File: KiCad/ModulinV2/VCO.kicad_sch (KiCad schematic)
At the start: 87 parts, among them Q1 MMBFJ201, Q2 MMBFJ201, SW3 SW_SPDT_MSM

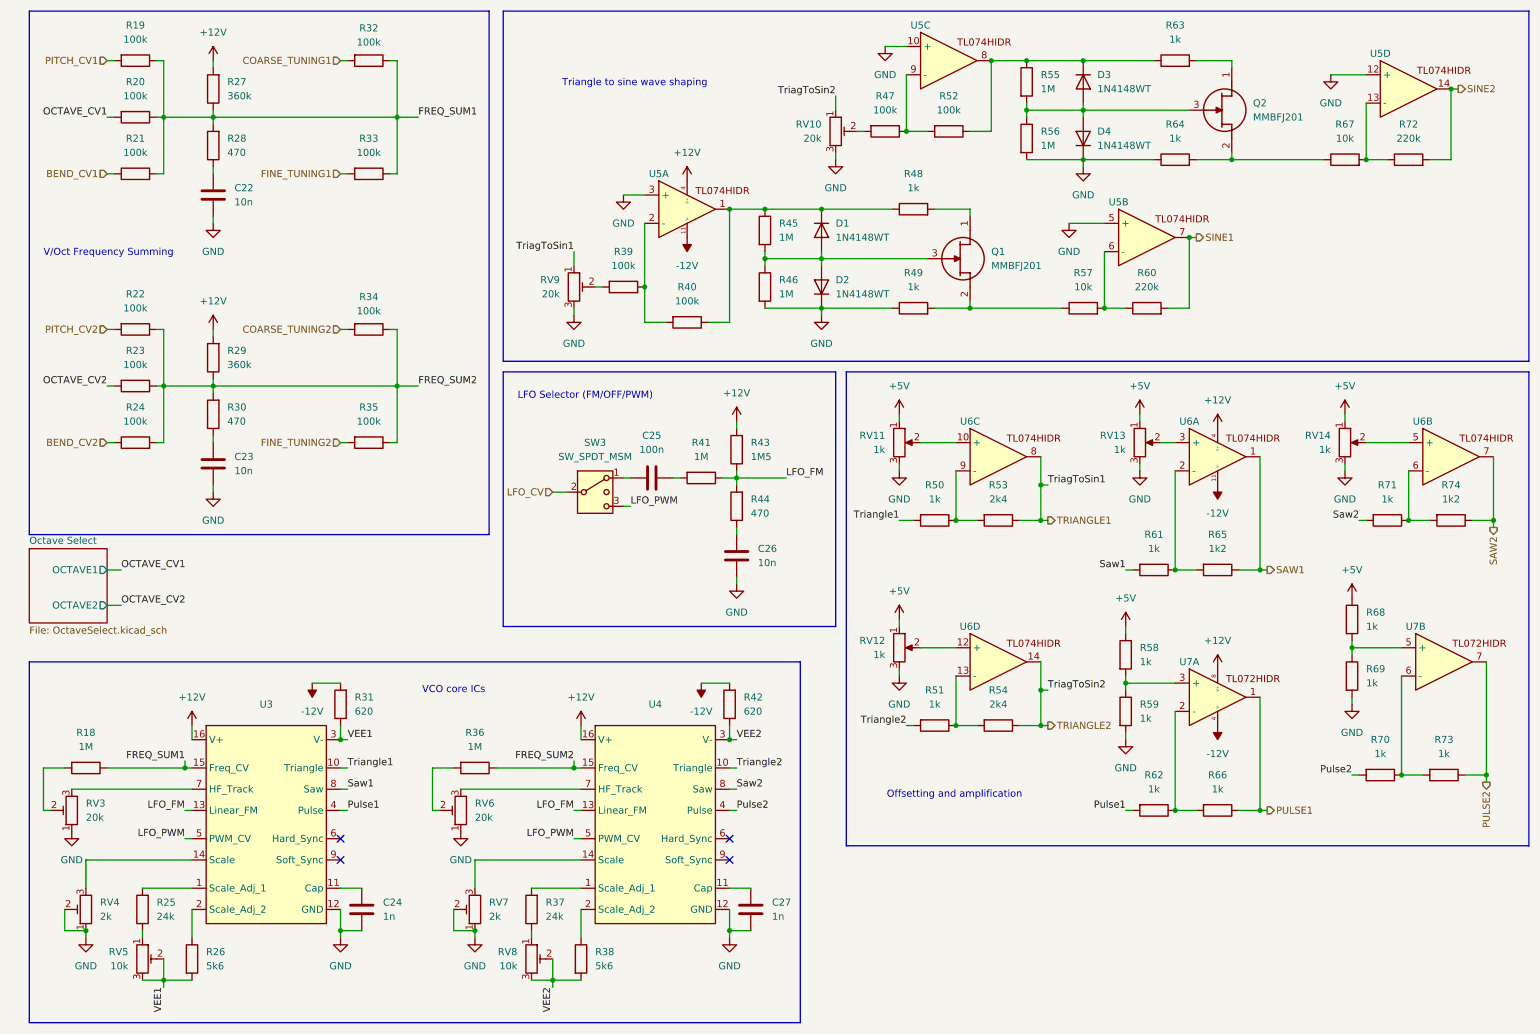
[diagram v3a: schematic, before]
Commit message: Fleshed out the waveform select schematic a bit + general cleanup
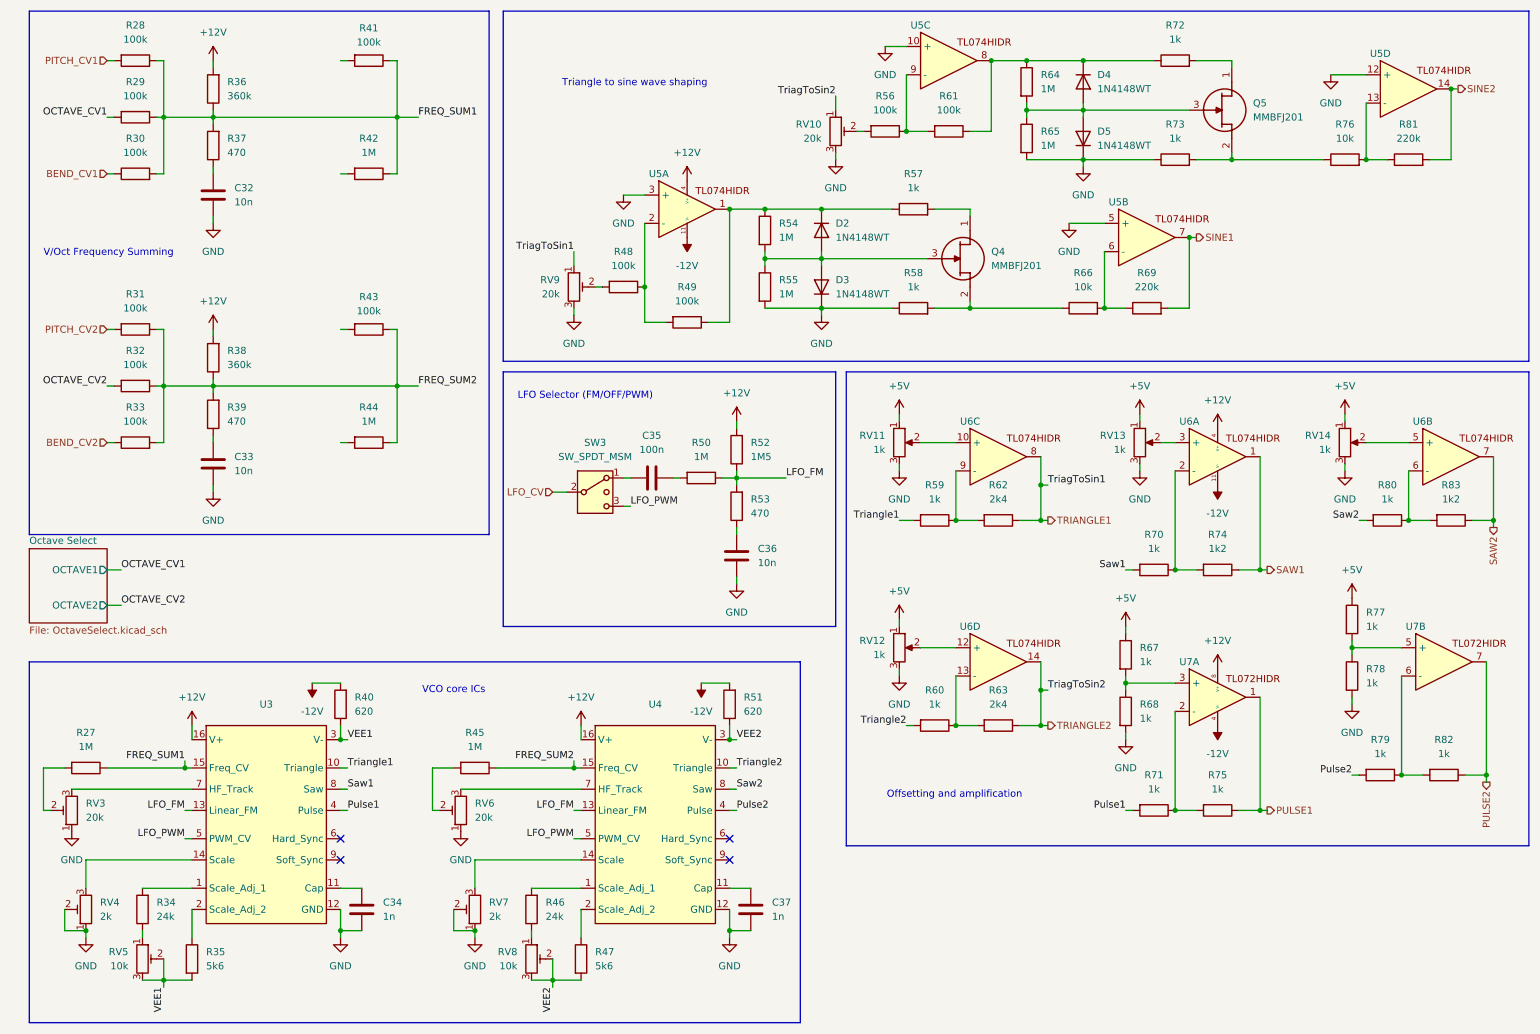
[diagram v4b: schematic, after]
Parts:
- R42: renamed from R33; value 100k -> 1M
- R44: renamed from R35; value 100k -> 1M
- renumbered C22 to C32, C23 to C33, C24 to C34, C25 to C35, C26 to C36, C27 to C37, D1 to D2, D2 to D3, D3 to D4, D4 to D5, Q1 to Q4, Q2 to Q5, R18 to R27, R19 to R28, R20 to R29, R21 to R30, R22 to R31, R23 to R32, R24 to R33, R25 to R34, R26 to R35, R27 to R36, R28 to R37, R29 to R38, R30 to R39, R31 to R40, R32 to R41, R34 to R43, R36 to R45, R37 to R46, R38 to R47, R39 to R48, R40 to R49, R41 to R50, R42 to R51, R43 to R52, R44 to R53, R45 to R54, R46 to R55, R47 to R56, R48 to R57, R49 to R58, R50 to R59, R51 to R60, R52 to R61, R53 to R62, R54 to R63, R55 to R64, R56 to R65, R57 to R66, R58 to R67, R59 to R68, R60 to R69, R61 to R70, R62 to R71, R63 to R72, R64 to R73, R65 to R74, R66 to R75, R67 to R76, R68 to R77, R69 to R78, R70 to R79, R71 to R80, R72 to R81, R73 to R82, R74 to R83
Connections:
- net COARSE_TUNING1: no longer names the net of R41.2
- net COARSE_TUNING2: no longer names the net of R43.2
- net FINE_TUNING1: no longer names the net of R42.2
- net FINE_TUNING2: no longer names the net of R44.2

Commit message: Added initial power supply schematic and modified MCU components
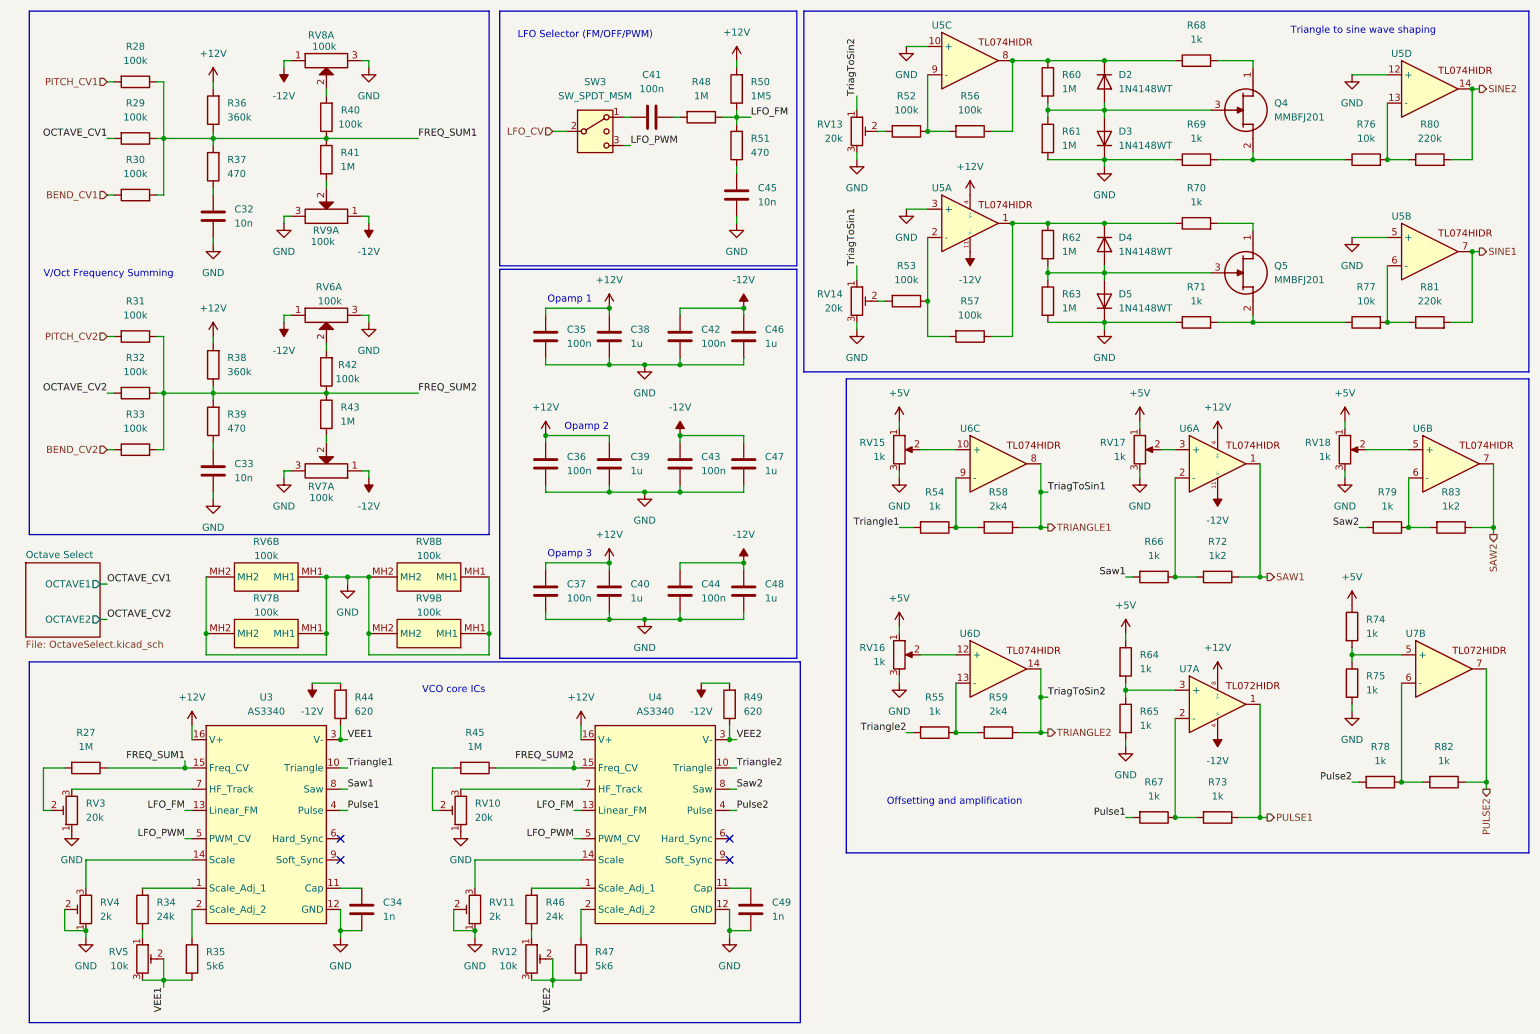
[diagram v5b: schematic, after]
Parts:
- added C35, C36, C37, C42, C43, C44: 100n, symbol Device:C
- added C38, C39, C40, C46, C47, C48: 1u, symbol Device:C
- added RV6, RV7, RV8, RV9: 100k, symbol PTV09A-4025F-B104:PTV09A-4025F-B104_Alt
- U3, U4: value ~ -> AS3340
- renumbered C35 to C41, C36 to C45, C37 to C49, D4 to D2, D5 to D3, D2 to D4, D3 to D5, Q5 to Q4, Q4 to Q5, R41 to R40, R42 to R41, R43 to R42, R44 to R43, R40 to R44, R50 to R48, R51 to R49, R52 to R50, R53 to R51, R56 to R52, R48 to R53, R59 to R54, R60 to R55, R61 to R56, R49 to R57, R62 to R58, R63 to R59, R64 to R60, R65 to R61, R54 to R62, R55 to R63, R67 to R64, R68 to R65, R70 to R66, R71 to R67, R72 to R68, R73 to R69, R57 to R70, R58 to R71, R74 to R72, R75 to R73, R77 to R74, R78 to R75, R66 to R77, R79 to R78, R80 to R79, R81 to R80, R69 to R81, RV6 to RV10, RV7 to RV11, RV8 to RV12, RV10 to RV13, RV9 to RV14, RV11 to RV15, RV12 to RV16, RV13 to RV17, RV14 to RV18
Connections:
- net +12V: now also C35.2, C36.2, C37.2, C38.2, C39.2, C40.2
- net -12V: now also C42.2, C43.2, C44.2, C46.2, C47.2, C48.2, RV6.1, RV7.1, RV8.1, RV9.1
- net GND: now also C35.1, C36.1, C37.1, C38.1, C39.1, C40.1, C42.1, C43.1, C44.1, C46.1, C47.1, C48.1, RV6.3, RV6.MH1, RV6.MH2, RV7.3, RV7.MH1, RV7.MH2, RV8.3, RV8.MH1, RV8.MH2, RV9.3, RV9.MH1, RV9.MH2
- net at R43.2: now also RV7.2
- net at R41.2: now also RV9.2
- net at R40.2: now also RV8.2
- net at R42.2: now also RV6.2
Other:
- note added: "Opamp 1"
- note added: "Opamp 2"
- note added: "Opamp 3"
- moved on the sheet: C32, C33, C41, C45, D2, D3, D4, D5, Q4, Q5, R28, R29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

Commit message: Designed ADSR and better tuning schematics with digital/manual capability
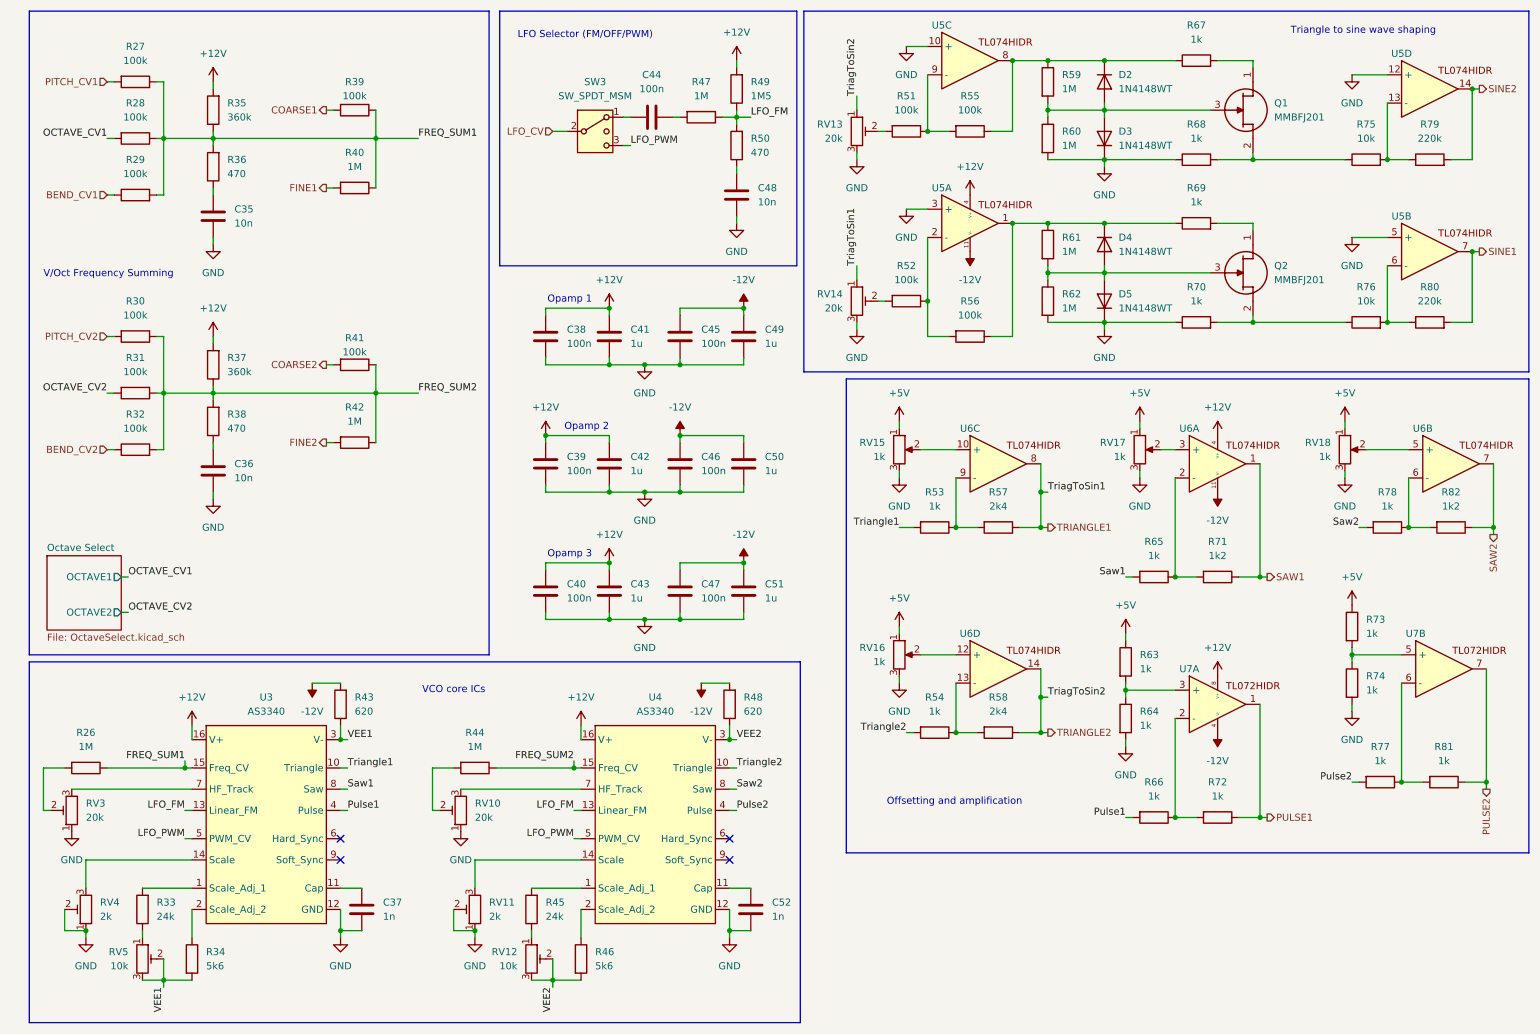
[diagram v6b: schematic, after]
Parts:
- removed RV6, RV7, RV8, RV9: 100k, symbol PTV09A-4025F-B104:PTV09A-4025F-B104_Alt
- renumbered C32 to C35, C33 to C36, C34 to C37, C35 to C38, C36 to C39, C37 to C40, C38 to C41, C39 to C42, C40 to C43, C41 to C44, C42 to C45, C43 to C46, C44 to C47, C45 to C48, C46 to C49, C47 to C50, C48 to C51, C49 to C52, Q4 to Q1, Q5 to Q2, R27 to R26, R28 to R27, R29 to R28, R30 to R29, R31 to R30, R32 to R31, R33 to R32, R34 to R33, R35 to R34, R36 to R35, R37 to R36, R38 to R37, R39 to R38, R40 to R39, R41 to R40, R42 to R41, R43 to R42, R44 to R43, R45 to R44, R46 to R45, R47 to R46, R48 to R47, R49 to R48, R50 to R49, R51 to R50, R52 to R51, R53 to R52, R54 to R53, R55 to R54, R56 to R55, R57 to R56, R58 to R57, R59 to R58, R60 to R59, R61 to R60, R62 to R61, R63 to R62, R64 to R63, R65 to R64, R66 to R65, R67 to R66, R68 to R67, R69 to R68, R70 to R69, R71 to R70, R72 to R71, R73 to R72, R74 to R73, R75 to R74, R76 to R75, R77 to R76, R78 to R77, R79 to R78, R80 to R79, R81 to R80, R82 to R81, R83 to R82
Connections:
- net FINE2: now reaches R42.2
- net FINE1: now reaches R40.2
- net COARSE1: now reaches R39.2
- net COARSE2: now reaches R41.2
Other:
- moved on the sheet: R39, R40, R41, R42

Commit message: Added 4k7 pullups to I2C lines
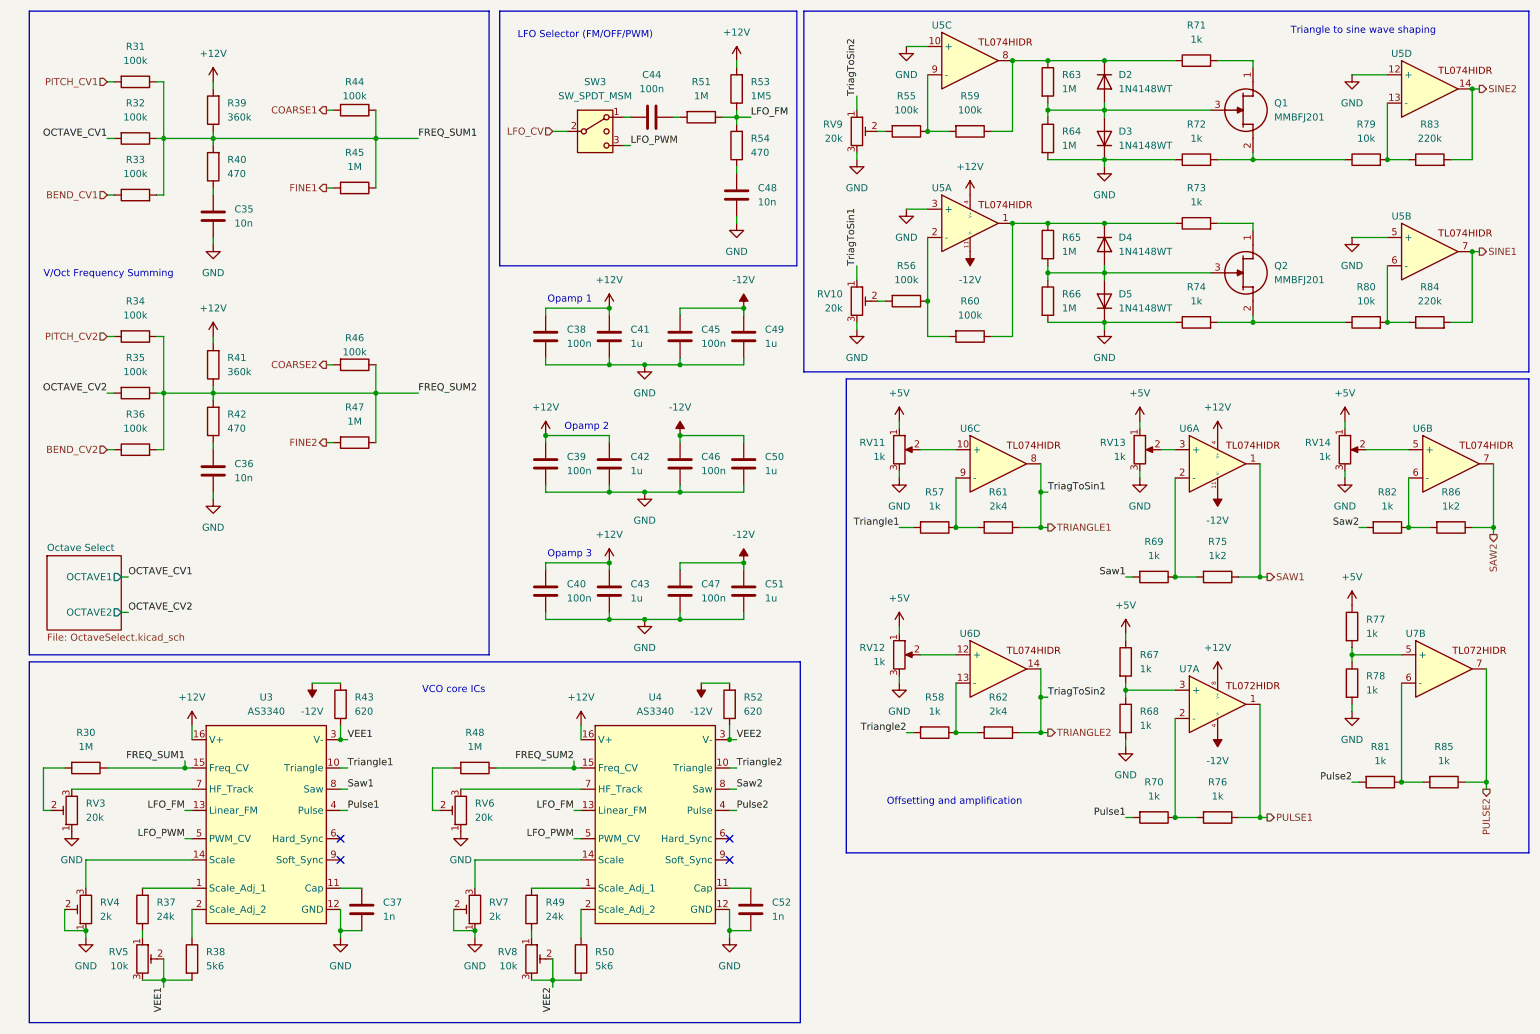
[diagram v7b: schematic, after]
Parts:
- renumbered R26 to R30, R27 to R31, R28 to R32, R29 to R33, R30 to R34, R31 to R35, R32 to R36, R33 to R37, R34 to R38, R35 to R39, R36 to R40, R37 to R41, R38 to R42, R39 to R44, R40 to R45, R41 to R46, R42 to R47, R44 to R48, R45 to R49, R46 to R50, R47 to R51, R48 to R52, R49 to R53, R50 to R54, R51 to R55, R52 to R56, R53 to R57, R54 to R58, R55 to R59, R56 to R60, R57 to R61, R58 to R62, R59 to R63, R60 to R64, R61 to R65, R62 to R66, R63 to R67, R64 to R68, R65 to R69, R66 to R70, R67 to R71, R68 to R72, R69 to R73, R70 to R74, R71 to R75, R72 to R76, R73 to R77, R74 to R78, R75 to R79, R76 to R80, R77 to R81, R78 to R82, R79 to R83, R80 to R84, R81 to R85, R82 to R86, RV14 to RV10, RV15 to RV11, RV16 to RV12, RV17 to RV13, RV18 to RV14, RV10 to RV6, RV11 to RV7, RV12 to RV8, RV13 to RV9
